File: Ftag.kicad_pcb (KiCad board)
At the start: 2 copper layers, 34.9 x 29.2 mm, 25 parts, among them P1 USB_OTG, P2 CONN_10X2, U1 FT232H, U2 TXB0108, X1 12 MHz

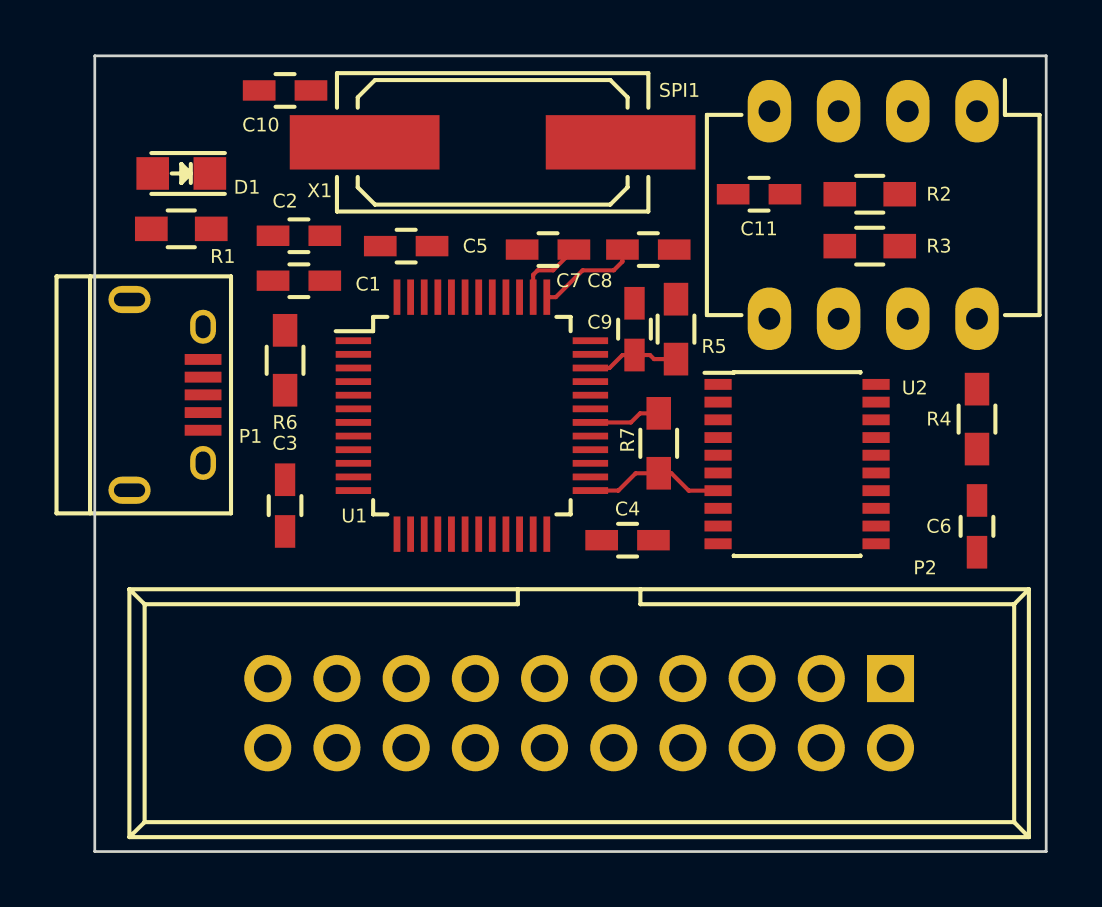
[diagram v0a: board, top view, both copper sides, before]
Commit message: Added some routing
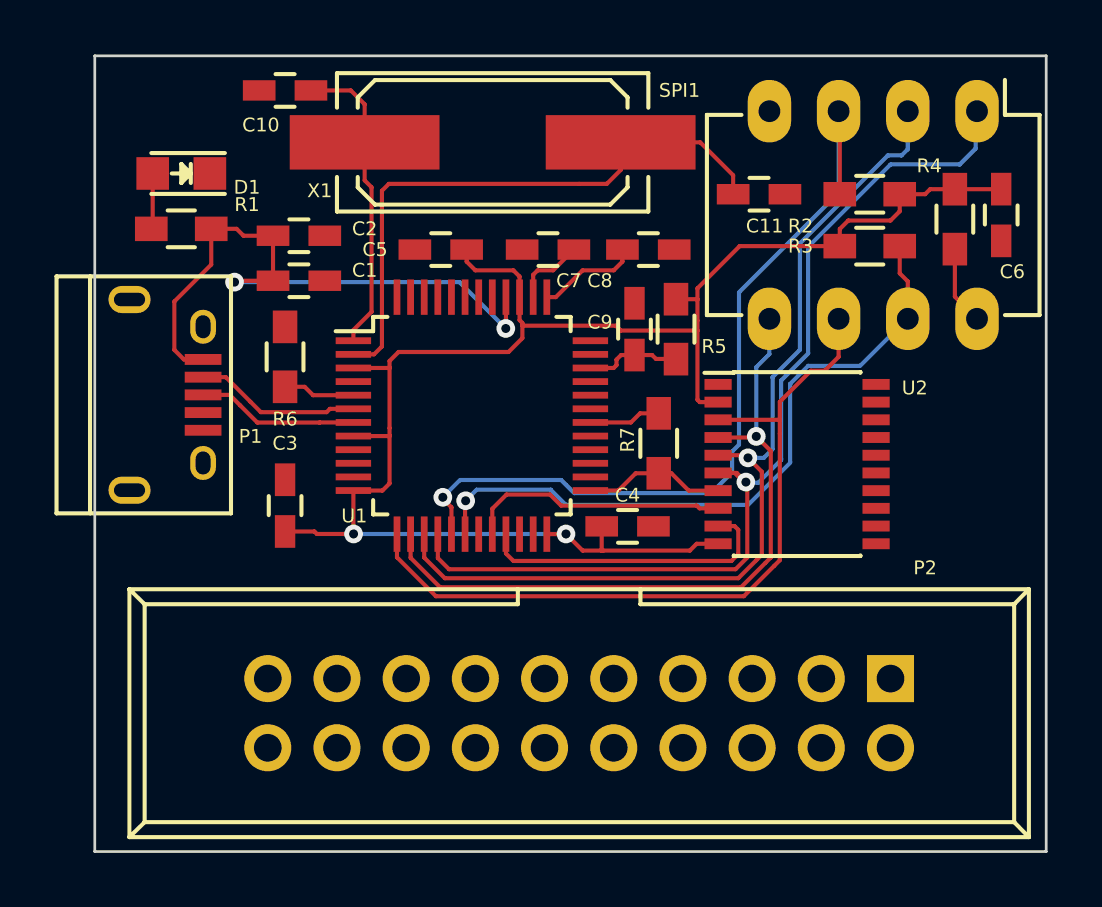
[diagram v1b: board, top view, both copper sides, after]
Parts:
- moved C6 11.5 mm to (176.1, 74.4)
- moved R4 7.39 mm to (174.4, 74.6), turned to 270 degrees
- moved C5 1.28 mm to (155.6, 75.7), turned to 180 degrees
- moved C4 0.51 mm to (162.4, 85.9)
- moved R6 0.13 mm to (149.9, 79.6)
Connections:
- P2 pad 5: (no net) -> /TDI
- U2 pad 17: (no net) -> /TDI
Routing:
- net +3V3: track 0.00 -> 63.9 mm, vias 0 -> 2
- net /CTS/TMS/CS: track 0.02 -> 36.2 mm, vias 0 -> 1
- net /RTS/TDO/DI: track 0.00 -> 34.6 mm, vias 0 -> 1
- net /DTR/OE/WP: track 0.00 -> 30.8 mm, vias 0 -> 1
- net /TX/TCK/SK: track 0.00 -> 28.4 mm
- net /RX/TDI/DO: track 0.00 -> 25.6 mm, vias 0 -> 1
- net /DSR/TP/HOLD: track 0.00 -> 25.2 mm, vias 0 -> 1
- net +5V: track 0.00 -> 23.5 mm, vias 0 -> 2
- net Net-(C11-Pad1): track 0.00 -> 22.3 mm
- net Net-(C10-Pad1): track 0.00 -> 11.2 mm
- net /TRSTo: track 0.00 -> 11.1 mm
- net /RI/RTCK/: track 0.00 -> 9.65 mm
- net /D-: track 0.00 -> 6.10 mm
- net /D+: track 0.00 -> 5.94 mm
- net Net-(R4-Pad2): track 0.00 -> 2.89 mm
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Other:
- board text added: "FTAG"
- board text added: "Power"

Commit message: Finished preliminary layout
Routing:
- net GND: track 0.00 -> 34.6 mm, vias 0 -> 4
- net /SRST: track 0.00 -> 21.5 mm, vias 0 -> 1
- net /TDO: track 0.00 -> 21.2 mm
- net /TCK: track 0.00 -> 16.1 mm, vias 0 -> 1
- net /RTCK: track 0.00 -> 15.1 mm, vias 0 -> 1
- net /VCCIO: track 0.00 -> 14.2 mm
- net /TMS: track 0.00 -> 13.3 mm
- net /TDI: track 0.00 -> 11.2 mm, vias 0 -> 1
- net /TRST: track 0.00 -> 6.87 mm
- added copper zone on B.Cu, net GND
- added copper zone on F.Cu, net GND

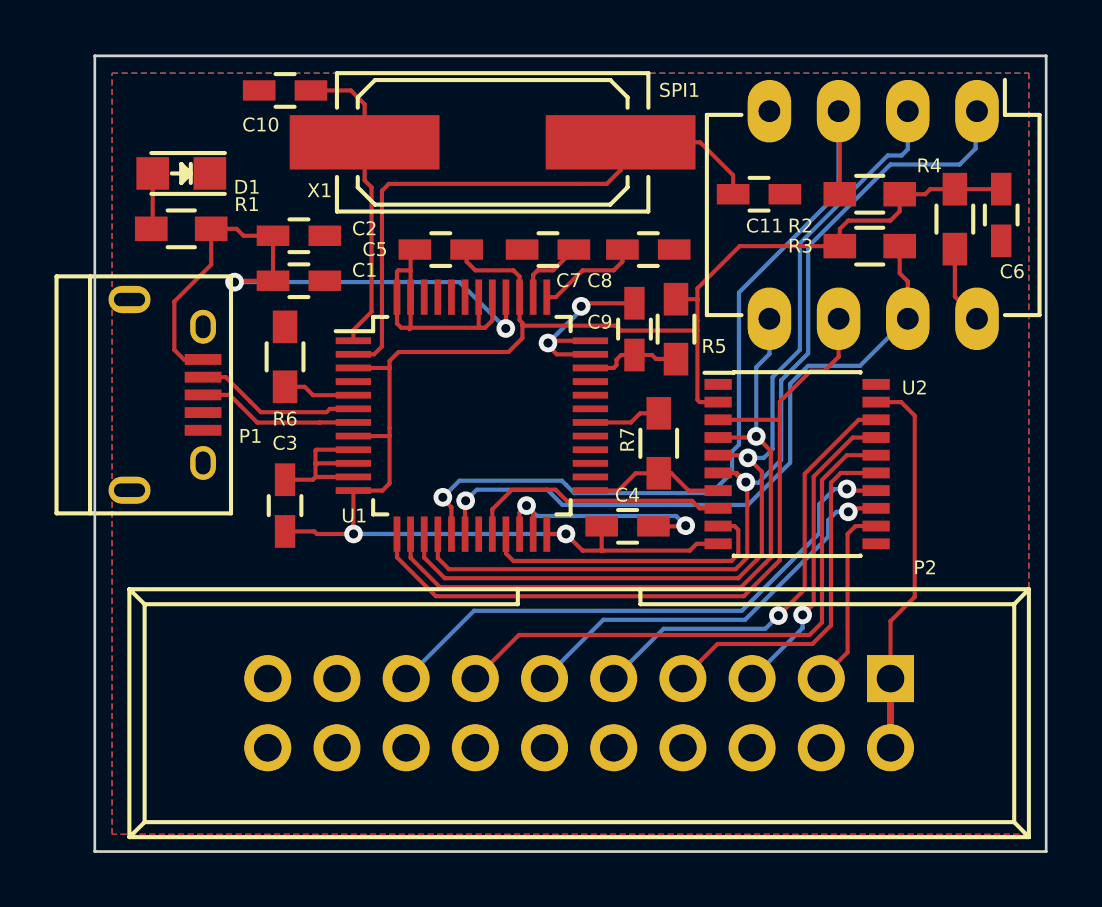
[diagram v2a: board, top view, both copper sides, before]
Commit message: Added via stitching
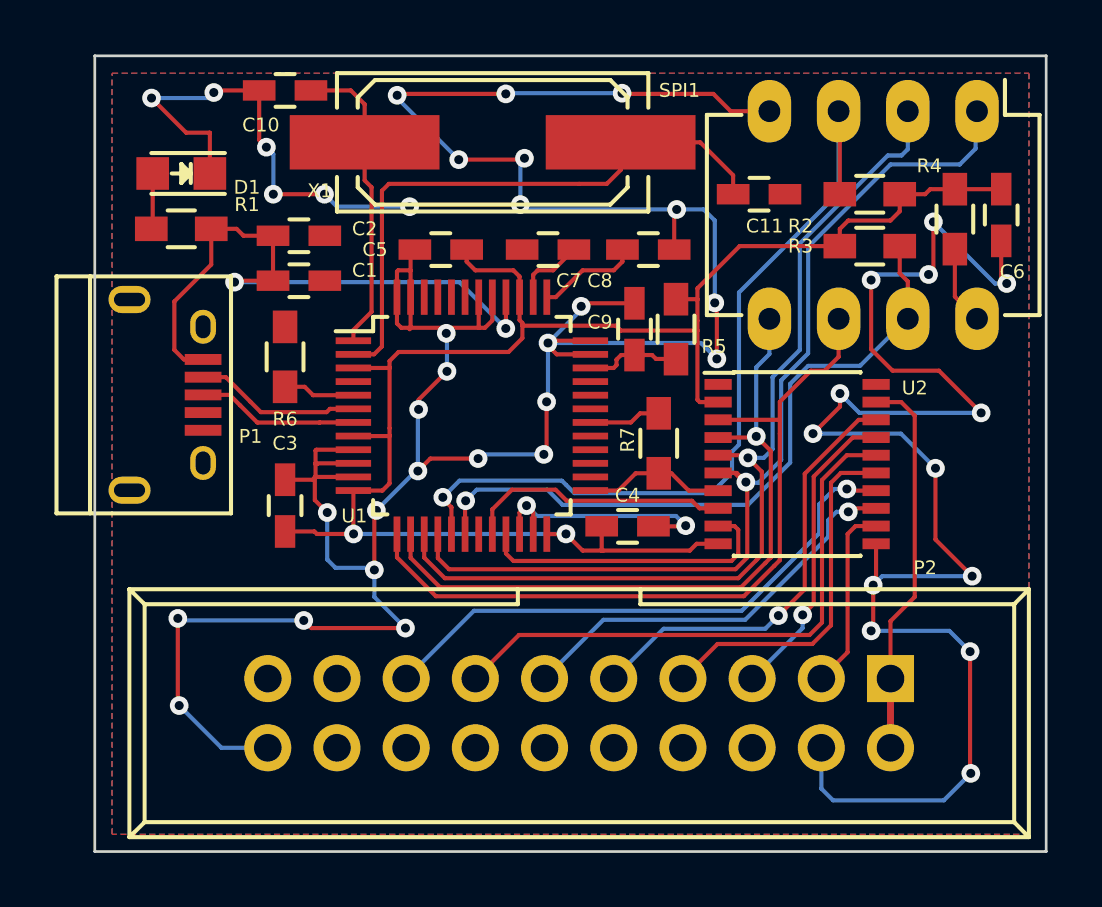
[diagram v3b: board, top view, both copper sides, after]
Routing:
- net GND: track 34.6 -> 197.5 mm, vias 4 -> 46

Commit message: Added silkscreen pinout
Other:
- board text added: "JTAG/RS232/SPI"
- board text added: "RTCK/RI"
- board text added: "SRST"
- board text added: "TCK/TX/SK"
- board text added: "TDI/RX/DO"
- board text added: "TDO/RTS/DI"
- board text added: "TMS/CTS/CS"
- board text added: "TRST"
- board text added: "Vcc IO"
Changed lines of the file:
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@@
     (area 139.4106 61.92 190.550715 97.840001)
     (thickness 1.6)
-    (drawings 8)
+    (drawings 17)
     (tracks 542)
     (zones 0)
@@
     (35 F.Paste user)
     (36 B.SilkS user)
-    (37 F.SilkS user hide)
+    (37 F.SilkS user)
     (38 B.Mask user)
     (39 F.Mask user)
@@
     (uvia_min_size 0)
     (uvia_min_drill 0)
-    (pcb_text_width 0.3)
-    (pcb_text_size 1.5 1.5)
+    (pcb_text_width 0.254)
+    (pcb_text_size 1.016 1.016)
     (mod_edge_width 0.15)
     (mod_text_size 1 1)
@@
     (pad_to_mask_clearance 0)
     (aux_axis_origin 0 0)
-    (visible_elements FFFFFF7F)
+    (visible_elements FFFFFFFF)
     (pcbplotparams
       (layerselection 0x010f0_80000001)
@@
     )
   )
+  (gr_text "Vcc IO" (at 172.085 89.535 270) (layer B.SilkS)
+    (effects (font (size 1.016 1.016) (thickness 0.254)) (justify left mirror))
+  )
+  (gr_text TCK/TX/SK (at 161.925 89.535 270) (layer B.SilkS)
+    (effects (font (size 1.016 1.016) (thickness 0.254)) (justify left mirror))
+  )
+  (gr_text TMS/CTS/CS (at 164.465 89.535 270) (layer B.SilkS)
+    (effects (font (size 1.016 1.016) (thickness 0.254)) (justify left mirror))
+  )
+  (gr_text TDI/RX/DO (at 167.005 89.535 270) (layer B.SilkS)
+    (effects (font (size 1.016 1.016) (thickness 0.254)) (justify left mirror))
+  )
+  (gr_text TRST (at 169.545 89.535 270) (layer B.SilkS)
+    (effects (font (size 1.016 1.016) (thickness 0.254)) (justify left mirror))
+  )
+  (gr_text RTCK/RI (at 159.385 89.535 270) (layer B.SilkS)
+    (effects (font (size 1.016 1.016) (thickness 0.254)) (justify left mirror))
+  )
+  (gr_text TDO/RTS/DI (at 156.845 89.535 270) (layer B.SilkS)
+    (effects (font (size 1.016 1.016) (thickness 0.254)) (justify left mirror))
+  )
+  (gr_text SRST (at 154.305 89.535 270) (layer B.SilkS)
+    (effects (font (size 1.016 1.016) (thickness 0.254)) (justify left mirror))
+  )
+  (gr_text JTAG/RS232/SPI (at 150.495 89.535 270) (layer B.SilkS)
+    (effects (font (size 1.016 1.016) (thickness 0.254)) (justify left mirror))
+  )
   (gr_text Power (at 146.05 71.1454) (layer F.Mask)
